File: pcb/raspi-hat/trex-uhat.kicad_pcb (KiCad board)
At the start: 2 copper layers, 89.5 x 30 mm, 23 parts, among them J1 Conn_01x08_Female, J10 RAIL2, J2 RPi_GPIO, J3 Conn_01x03_Female, J4 DFPLAYER_MINI, J5 RAIL1, J6 Conn_01x04_Female, J7 AudioJack3, J8 Jack-DC, J9 Conn_01x05_Female

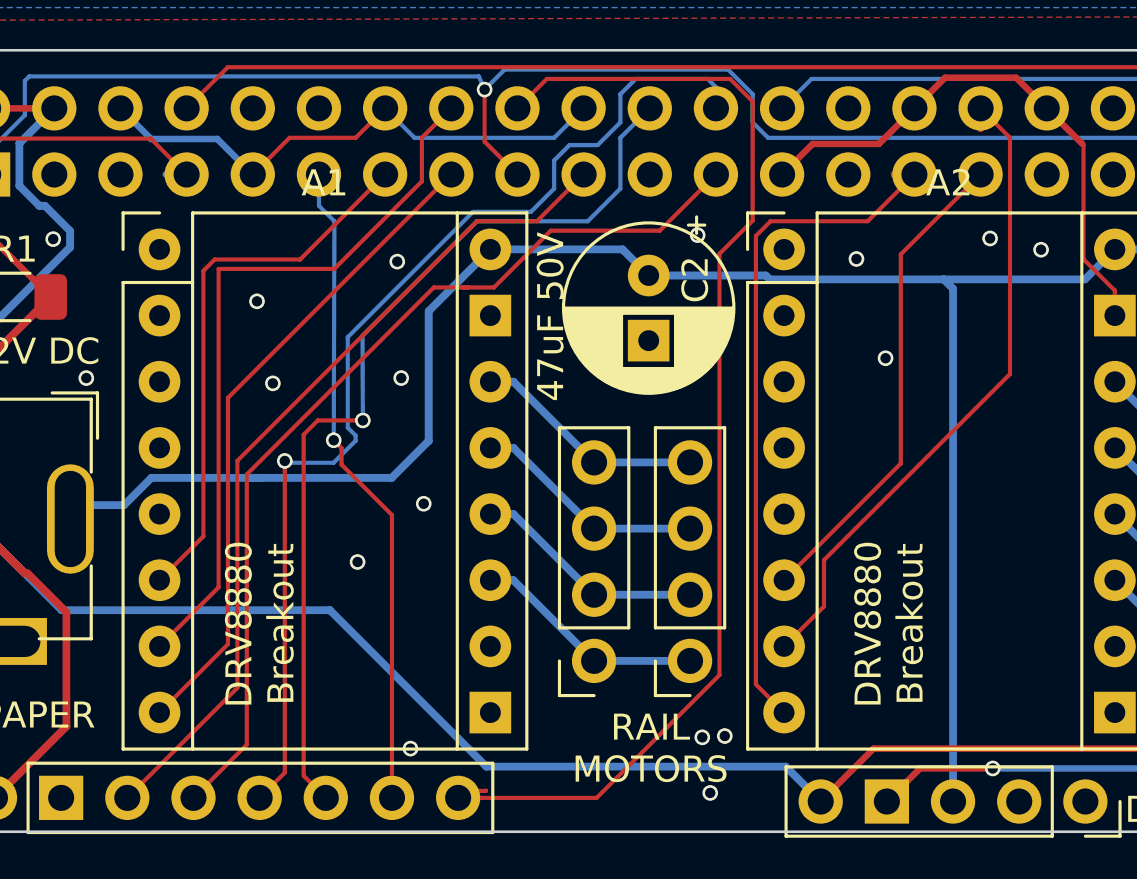
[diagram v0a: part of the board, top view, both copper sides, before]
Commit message: feat(pcb): DRV8825 support
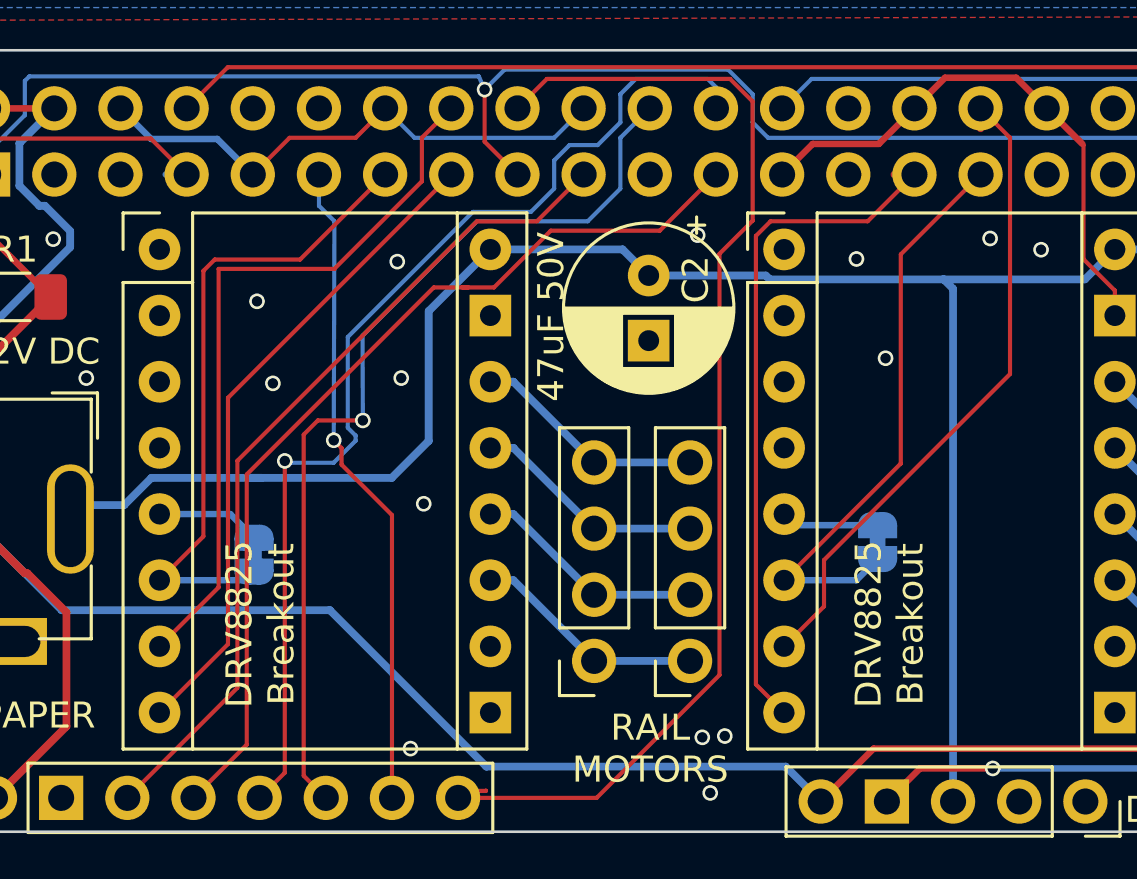
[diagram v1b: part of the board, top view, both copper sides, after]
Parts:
- added JP1: Jumper, Jumper:SolderJumper-2_P1.3mm_Bridged_RoundedPad1.0x1.5mm, B.Cu at (31.1, 43.9)
- added JP2: Jumper, Jumper:SolderJumper-2_P1.3mm_Bridged_RoundedPad1.0x1.5mm, B.Cu at (55.0, 43.4)
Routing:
- net Net-(A1-Pad5): track 0.00 -> 4.00 mm
- net /STP2_~SLP: track 18.7 -> 22.6 mm
- net Net-(A2-Pad5): track 0.00 -> 3.77 mm
- net /STP1_~SLP: track 21.1 -> 24.8 mm
- net GND: vias 26 -> 25
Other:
- board text added: "DRV8825 Breakout"
- board text removed: "DRV8880 Breakout"
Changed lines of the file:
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@@
     (thickness 1.6)
     (drawings 32)
-    (tracks 296)
+    (tracks 303)
     (zones 0)
-    (modules 23)
+    (modules 25)
     (nets 69)
   )
@@
     (add_net "Net-(J9-Pad2)")
   )
+  (module Jumper:SolderJumper-2_P1.3mm_Bridged_RoundedPad1.0x1.5mm (layer B.Cu)
+    (at 55.0164 43.3809 270)
+    (descr "SMD Solder Jumper, 1x1.5mm, rounded Pads, 0.3mm gap, bridged with 1 copper strip")
+    (tags "solder jumper open")
+    (attr virtual)
+    (fp_text reference JP2 (at 0 1.8 270) (layer B.SilkS)
+      (effects (font (size 1 1) (thickness 0.1)) (justify mirror))
+    )
+    (fp_text value Jumper (at 0 -1.9 270) (layer B.Fab)
+      (effects (font (size 1 1) (thickness 0.15)) (justify mirror))
+    )
+    (fp_poly (pts (xy 0.25 0.3) (xy -0.25 0.3) (xy -0.25 -0.3) (xy 0.25 -0.3)) (layer B.Cu) (width 0))
+    (fp_line (start 1.65 -1.25) (end -1.65 -1.25) (layer B.CrtYd) (width 0.05))
+    (fp_line (start 1.65 -1.25) (end 1.65 1.25) (layer B.CrtYd) (width 0.05))
+    (fp_line (start -1.65 1.25) (end -1.65 -1.25) (layer B.CrtYd) (width 0.05))
+    (fp_line (start -1.65 1.25) (end 1.65 1.25) (layer B.CrtYd) (width 0.05))
+    (fp_line (start -0.7 1) (end 0.7 1) (layer B.SilkS) (width 0.12))
+    (fp_line (start 1.4 0.3) (end 1.4 -0.3) (layer B.SilkS) (width 0.12))
+    (fp_line (start 0.7 -1) (end -0.7 -1) (layer B.SilkS) (width 0.12))
+    (fp_line (start -1.4 -0.3) (end -1.4 0.3) (layer B.SilkS) (width 0.12))
+    (fp_arc (start -0.7 0.3) (end -0.7 1) (angle 90) (layer B.SilkS) (width 0.12))
+    (fp_arc (start -0.7 -0.3) (end -1.4 -0.3) (angle 90) (layer B.SilkS) (width 0.12))
+    (fp_arc (start 0.7 -0.3) (end 0.7 -1) (angle 90) (layer B.SilkS) (width 0.12))
+    (fp_arc (start 0.7 0.3) (end 1.4 0.3) (angle 90) (layer B.SilkS) (width 0.12))
+    (pad 1 smd custom (at -0.65 0 270) (size 1 0.5) (layers B.Cu B.Mask)
+      (net 48 "Net-(A2-Pad5)") (zone_connect 2)
+      (options (clearance outline) (anchor rect))
+      (primitives
+        (gr_circle (center 0 -0.25) (end 0.5 -0.25) (width 0))
+        (gr_circle (center 0 0.25) (end 0.5 0.25) (width 0))
+        (gr_poly (pts
+           (xy 0 0.75) (xy 0.5 0.75) (xy 0.5 -0.75) (xy 0 -0.75)) (width 0))
+      ))
+    (pad 2 smd custom (at 0.65 0 270) (size 1 0.5) (layers B.Cu B.Mask)
+      (net 67 /STP2_~SLP) (zone_connect 2)
+      (options (clearance outline) (anchor rect))
+      (primitives
+        (gr_circle (center 0 -0.25) (end 0.5 -0.25) (width 0))
+        (gr_circle (center 0 0.25) (end 0.5 0.25) (width 0))
+        (gr_poly (pts
+           (xy 0 0.75) (xy -0.5 0.75) (xy -0.5 -0.75) (xy 0 -0.75)) (width 0))
+      ))
+  )
+  (module Jumper:SolderJumper-2_P1.3mm_Bridged_RoundedPad1.0x1.5mm (layer B.Cu)
+    (at 31.0769 43.8658 270)
+    (descr "SMD Solder Jumper, 1x1.5mm, rounded Pads, 0.3mm gap, bridged with 1 copper strip")
+    (tags "solder jumper open")
+    (attr virtual)
+    (fp_text reference JP1 (at 0 1.8 90) (layer B.SilkS)
+      (effects (font (size 1 1) (thickness 0.1)) (justify mirror))
+    )
+    (fp_text value Jumper (at 0 -1.9 90) (layer B.Fab)
+      (effects (font (size 1 1) (thickness 0.15)) (justify mirror))
+    )
+    (fp_poly (pts (xy 0.25 0.3) (xy -0.25 0.3) (xy -0.25 -0.3) (xy 0.25 -0.3)) (layer B.Cu) (width 0))
+    (fp_line (start 1.65 -1.25) (end -1.65 -1.25) (layer B.CrtYd) (width 0.05))
+    (fp_line (start 1.65 -1.25) (end 1.65 1.25) (layer B.CrtYd) (width 0.05))
+    (fp_line (start -1.65 1.25) (end -1.65 -1.25) (layer B.CrtYd) (width 0.05))
+    (fp_line (start -1.65 1.25) (end 1.65 1.25) (layer B.CrtYd) (width 0.05))
+    (fp_line (start -0.7 1) (end 0.7 1) (layer B.SilkS) (width 0.12))
+    (fp_line (start 1.4 0.3) (end 1.4 -0.3) (layer B.SilkS) (width 0.12))
+    (fp_line (start 0.7 -1) (end -0.7 -1) (layer B.SilkS) (width 0.12))
+    (fp_line (start -1.4 -0.3) (end -1.4 0.3) (layer B.SilkS) (width 0.12))
+    (fp_arc (start -0.7 0.3) (end -0.7 1) (angle 90) (layer B.SilkS) (width 0.12))
+    (fp_arc (start -0.7 -0.3) (end -1.4 -0.3) (angle 90) (layer B.SilkS) (width 0.12))
+    (fp_arc (start 0.7 -0.3) (end 0.7 -1) (angle 90) (layer B.SilkS) (width 0.12))
+    (fp_arc (start 0.7 0.3) (end 1.4 0.3) (angle 90) (layer B.SilkS) (width 0.12))
+    (pad 1 smd custom (at -0.65 0 270) (size 1 0.5) (layers B.Cu B.Mask)
+      (net 38 "Net-(A1-Pad5)") (zone_connect 2)
+      (options (clearance outline) (anchor rect))
+      (primitives
+        (gr_circle (center 0 -0.25) (end 0.5 -0.25) (width 0))
+        (gr_circle (center 0 0.25) (end 0.5 0.25) (width 0))
+        (gr_poly (pts
+           (xy 0 0.75) (xy 0.5 0.75) (xy 0.5 -0.75) (xy 0 -0.75)) (width 0))
+      ))
+    (pad 2 smd custom (at 0.65 0 270) (size 1 0.5) (layers B.Cu B.Mask)
+      (net 65 /STP1_~SLP) (zone_connect 2)
+      (options (clearance outline) (anchor rect))
+      (primitives
+        (gr_circle (center 0 -0.25) (end 0.5 -0.25) (width 0))
+        (gr_circle (center 0 0.25) (end 0.5 0.25) (width 0))
+        (gr_poly (pts
+           (xy 0 0.75) (xy -0.5 0.75) (xy -0.5 -0.75) (xy 0 -0.75)) (width 0))
+      ))
+  )
   (module RPi_Hat:DFPlayer_Mini (layer F.Cu)
     (at 80.25 44 90)
@@
     (descr "Pololu Breakout 16-pin 15.2x20.3mm 0.6x0.8\\")
     (tags "Pololu Breakout")
-    (fp_text reference A1 (at 6.35 -2.54) (layer F.SilkS)
+    (fp_text reference A1 (at 6.35 -2.54) (layer F.SilkS) hide
       (effects (font (size 1 1) (thickness 0.15)))
     )
@@
     (descr "Pololu Breakout 16-pin 15.2x20.3mm 0.6x0.8\\")
     (tags "Pololu Breakout")
-    (fp_text reference A2 (at 6.35 -2.54) (layer F.SilkS)
+    (fp_text reference A2 (at 6.35 -2.54) (layer F.SilkS) hide
       (effects (font (size 1 1) (thickness 0.15)))
     )
@@
     (effects (font (size 1 1) (thickness 0.15)) (justify mirror))
   )
-  (gr_text "DRV8880\nBreakout" (at 31.3182 46.5328 90) (layer F.SilkS)
+  (gr_text "DRV8825\nBreakout" (at 31.3182 46.5328 90) (layer F.SilkS)
     (effects (font (size 1 1) (thickness 0.15)))
   )
-  (gr_text "DRV8880\nBreakout" (at 55.4736 46.5328 90) (layer F.SilkS)
+  (gr_text "DRV8825\nBreakout" (at 55.4736 46.5328 90) (layer F.SilkS)
     (effects (font (size 1 1) (thickness 0.15)))
   )
@@
   (via (at 31.8008 37.2872) (size 0.6) (drill 0.4) (layers F.Cu B.Cu) (net 19))
   (via (at 36.576 32.6136) (size 0.6) (drill 0.4) (layers F.Cu B.Cu) (net 19))
-  (via (at 35.052 44.1452) (size 0.6) (drill 0.4) (layers F.Cu B.Cu) (net 19))
   (segment (start 64.125 33.725) (end 64.125 34.685) (width 0.16) (layer F.Cu) (net 19) (status 20))
   (segment (start 62.919999 32.519999) (end 64.125 33.725) (width 0.16) (layer F.Cu) (net 19))
@@
   (segment (start 41.035 39.765) (end 40.15 39.765) (width 0.3) (layer B.Cu) (net 37) (status 20))
   (segment (start 44.1325 42.8625) (end 41.035 39.765) (width 0.3) (layer B.Cu) (net 37) (status 10))
+  (segment (start 30.1661 42.305) (end 27.45 42.305) (width 0.25) (layer B.Cu) (net 38))
+  (segment (start 31.0769 43.2158) (end 30.1661 42.305) (width 0.25) (layer B.Cu) (net 38))
   (segment (start 40.2 42.355) (end 40.15 42.305) (width 0.25) (layer B.Cu) (net 39) (status 30))
   (segment (start 47.8155 45.4025) (end 44.1325 45.4025) (width 0.3) (layer B.Cu) (net 39) (status 30))
@@
   (segment (start 66.905 42.545) (end 69.2785 42.545) (width 0.3) (layer B.Cu) (net 47) (status 20))
   (segment (start 64.125 39.765) (end 66.905 42.545) (width 0.3) (layer B.Cu) (net 47) (status 10))
+  (segment (start 51.8509 42.7309) (end 51.425 42.305) (width 0.25) (layer B.Cu) (net 48))
+  (segment (start 55.0164 42.7309) (end 51.8509 42.7309) (width 0.25) (layer B.Cu) (net 48))
   (segment (start 64.175 42.305) (end 64.125 42.305) (width 0.25) (layer B.Cu) (net 49) (status 30))
   (segment (start 66.905 45.085) (end 69.2785 45.085) (width 0.3) (layer B.Cu) (net 49) (status 20))
@@
   (segment (start 29.1338 43.1612) (end 27.45 44.845) (width 0.16) (layer F.Cu) (net 65) (status 20))
   (segment (start 29.1338 32.968069) (end 29.1338 43.1612) (width 0.16) (layer F.Cu) (net 65))
+  (segment (start 30.7477 44.845) (end 31.0769 44.5158) (width 0.25) (layer B.Cu) (net 65))
+  (segment (start 27.45 44.845) (end 30.7477 44.845) (width 0.25) (layer B.Cu) (net 65))
   (segment (start 55.9054 40.3646) (end 51.425 44.845) (width 0.16) (layer F.Cu) (net 67) (status 20))
   (segment (start 55.9054 32.3346) (end 55.9054 40.3646) (width 0.16) (layer F.Cu) (net 67))
   (segment (start 58.97 29.27) (end 55.9054 32.3346) (width 0.16) (layer F.Cu) (net 67) (status 10))
+  (segment (start 54.2023 44.845) (end 55.0164 44.0309) (width 0.25) (layer B.Cu) (net 67))
+  (segment (start 51.425 44.845) (end 54.2023 44.845) (width 0.25) (layer B.Cu) (net 67))
   (zone (net 19) (net_name GND) (layer F.Cu) (hatch edge 0.508)
     (connect_pads (clearance 0.508))
